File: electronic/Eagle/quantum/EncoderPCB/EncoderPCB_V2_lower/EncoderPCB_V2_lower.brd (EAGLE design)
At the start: 150 x 30 mm, 20 parts, among them IC1 STM32F031K6T6

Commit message: progress on parametricEQ
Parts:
- added C5, C6, C7: 100nF, C_Sager_Bibliothek:C0603
- added C8: 10 uF, passive components:C1206
- added IC2: STM32F031K6T6, C_Sager_Bibliothek:QFP80P900X900X160-32N
- added PRG-CONN1: 90814-0204, electro_mechanical:MOLEX_90814-0204
- added R5, R6: 10k, passive components:R0603
- moved PRG-CONN 139.2 mm to (8.50, 23.9), flipped to the top, turned to 180 degrees
- moved I2C-CONN 96.8 mm to (38.7, 42.9), flipped to the top, turned to 180 degrees
- moved C3 26.4 mm to (128.8, 19.8), flipped to the top
- moved R8 25.8 mm to (81.5, 21.9), flipped to the top
- moved R9 25.8 mm to (78.3, 21.7), flipped to the top
- moved R10 25.8 mm to (73.4, 22.0), flipped to the top
- moved C1 25.3 mm to (115.5, 14.0), flipped to the top
- moved C2 25.3 mm to (116.1, 18.6), flipped to the top
- moved IC1 25.3 mm to (122.3, 17.2), flipped to the top
- moved R1 25.3 mm to (115.5, 16.0), flipped to the top
- moved C4 25.2 mm to (114.0, 19.3), flipped to the top
- moved R2 20.2 mm to (68.4, 21.7), flipped to the top
- moved R4 20.2 mm to (62.2, 21.8), flipped to the top
- moved R3 20.2 mm to (65.4, 21.9), flipped to the top
- moved R11 20.0 mm to (124.5, 10.6), flipped to the top
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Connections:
- net +3V3: now also C5.1, C6.1, C7.1, C8.1, IC2.1, IC2.17, IC2.5
- net ADRR.: now also IC2.3, R5.2
- net BOOT_0: now also IC2.31, R6.2
- net BUTTON_ENC1: now also IC2.28
- net BUTTON_ENC2: now also IC2.30
- net BUTTON_ENC3: now also IC2.2
- net B_ENC1: now also IC2.11
- net B_ENC2: now also IC2.14
- net B_ENC3: now also IC2.27
- net ENCODER1_A: now also IC2.18
- net ENCODER1_B: now also IC2.19
- net ENCODER2_A: now also IC2.6
- net ENCODER2_B: now also IC2.7
- net ENCODER3_A: now also IC2.12
- net ENCODER3_B: now also IC2.13
- net GND: now also C5.2, C6.2, C7.2, C8.2, IC2.16, IC2.32, PRG-CONN1.4, R5.1, R6.1
- net G_ENC1: now also IC2.10
- net G_ENC2: now also IC2.22
- net G_ENC3: now also IC2.26
- net I2C1_SCL: now also IC2.29
- net I2C1_SDA: now also IC2.20
- net NRST: now also IC2.4, PRG-CONN1.2
- net R_ENC1: now also IC2.9
- net R_ENC2: now also IC2.21
- net R_ENC3: now also IC2.15
- net SWCLK: now also IC2.24, PRG-CONN1.1
- net SWDIO: now also IC2.23, PRG-CONN1.3
- net USART1_RX1: now also IC2.25
- net USART1_TX: now also IC2.8
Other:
- board size 150 x 30 mm -> 130 x 45 mm

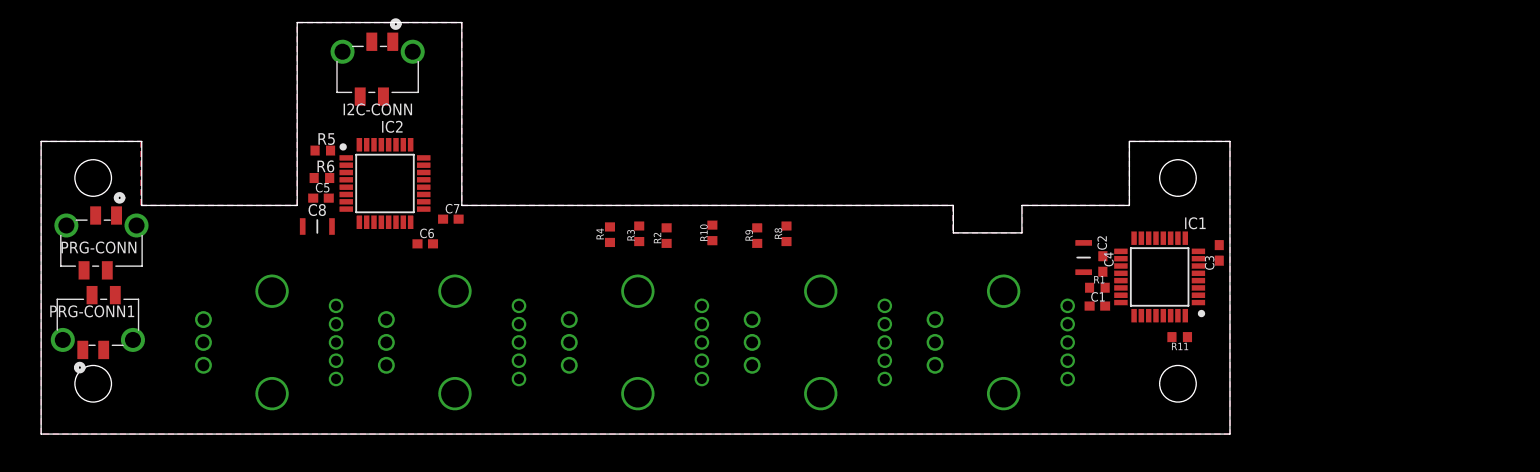
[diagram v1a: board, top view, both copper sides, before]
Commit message: finished EncoderPCB, Implemented Float OSC
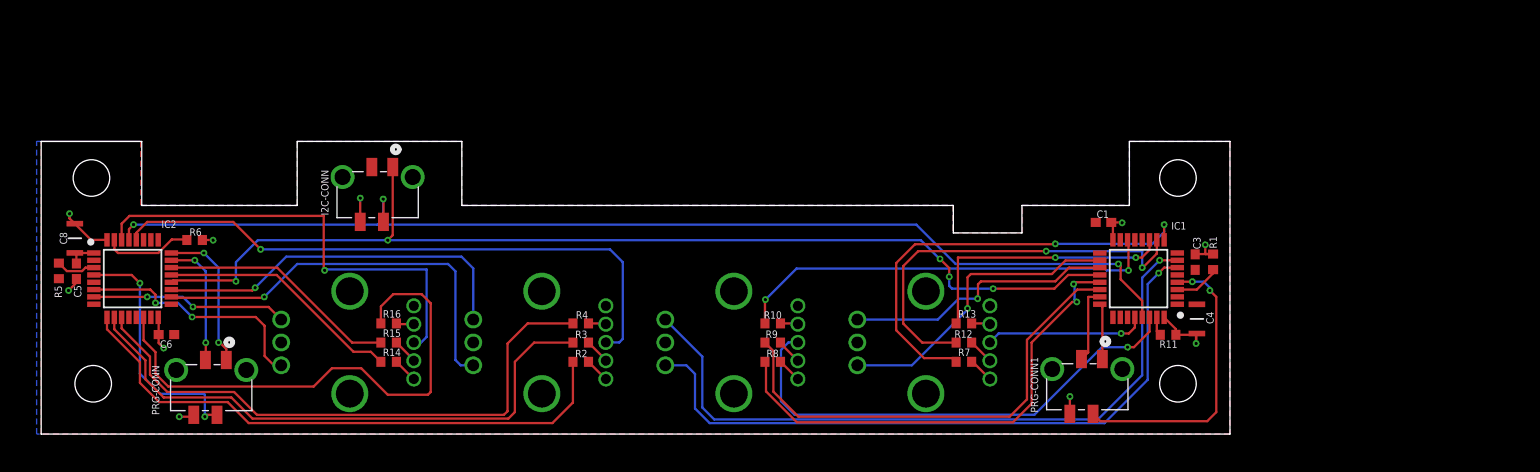
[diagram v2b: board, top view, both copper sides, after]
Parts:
- removed C2, C7: 100nF, C_Sager_Bibliothek:C0603
- removed S5: PEL12T-4225S-S1024, electro_mechanical:PEL12T4225SS1024
- added R12, R13, R14, R15, R16, R7: 51 R, passive components:R0603
- moved PRG-CONN1 112.0 mm to (116.3, 8.20), turned to 180 degrees
- moved S4 71.5 mm to (33.5, 10.0)
- moved R5 31.7 mm to (1.94, 17.8), turned to 90 degrees
- moved S1 31.5 mm to (96.5, 10.0)
- moved S2 30.5 mm to (75.5, 10.0)
- moved S3 30.5 mm to (54.5, 10.0)
- moved C6 30.0 mm to (13.7, 10.9), turned to 180 degrees
- moved IC2 29.5 mm to (10.0, 17.0)
- moved C5 27.9 mm to (3.85, 17.8), turned to 270 degrees
- moved C8 26.6 mm to (3.68, 21.4), turned to 90 degrees
- moved PRG-CONN 19.8 mm to (20.5, 8.10)
- moved R2 16.7 mm to (59.0, 7.90), turned to 0 degrees
- moved R6 15.5 mm to (16.8, 21.2), turned to 180 degrees
- moved C4 14.1 mm to (126.4, 12.6), turned to 270 degrees
- moved R8 14.1 mm to (80.0, 7.90), turned to 0 degrees
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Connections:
- removed net ADRR.: IC1.3, IC2.3, R1.2, R5.2
- removed net BOOT_0: IC1.31, IC2.31, R11.2, R6.2
- removed net BUTTON_ENC1: IC1.28, IC2.28, S1.3
- removed net BUTTON_ENC2: IC1.30, IC2.30
- removed net BUTTON_ENC3: IC1.2, IC2.2, S3.3
- removed net B_ENC1: IC1.11, IC2.11, R4.1
- removed net B_ENC2: IC1.14, IC2.14
- removed net B_ENC3: IC1.27, IC2.27, R10.1
- removed net ENCODER1_A: IC1.18, IC2.18, S1.A1
- removed net ENCODER1_B: IC1.19, IC2.19, S1.B1
- removed net ENCODER2_A: IC1.6, IC2.6
- removed net ENCODER2_B: IC1.7, IC2.7
- removed net ENCODER3_A: IC1.12, IC2.12, S3.A1
- removed net ENCODER3_B: IC1.13, IC2.13, S3.B1
- removed net G_ENC1: IC1.10, IC2.10, R3.1
- removed net G_ENC2: IC1.22, IC2.22
- removed net G_ENC3: IC1.26, IC2.26, R9.1
- removed net NRST: IC1.4, IC2.4, PRG-CONN.2, PRG-CONN1.2
- removed net R_ENC1: IC1.9, IC2.9, R2.1
- removed net R_ENC2: IC1.21, IC2.21
- removed net R_ENC3: IC1.15, IC2.15, R8.1
- removed net SWCLK: IC1.24, IC2.24, PRG-CONN.1, PRG-CONN1.1
- removed net SWDIO: IC1.23, IC2.23, PRG-CONN.3, PRG-CONN1.3
- removed net USART1_RX1: IC1.25, IC2.25
- removed net USART1_TX: IC1.8, IC2.8
- new net A_ADRR.: IC1.3, R1.2
- new net A_BOOT_0: IC1.31, R11.2
- new net A_BUTTON_ENC1: IC1.28, S1.3
- new net A_BUTTON_ENC2: IC1.30, S2.3
- new net A_BUTTON_ENC3: IC1.2
- new net A_B_ENC1: IC1.11, R13.1
- new net A_B_ENC2: IC1.14, R10.1
- new net A_B_ENC3: IC1.27
- new net A_ENCODER1_A: IC1.18, S1.A1
- new net A_ENCODER1_B: IC1.19, S1.B1
- new net A_ENCODER2_A: IC1.6, S2.A1
- new net A_ENCODER2_B: IC1.7, S2.B1
- new net A_ENCODER3_A: IC1.12
- new net A_ENCODER3_B: IC1.13
- new net A_G_ENC1: IC1.10, R12.1
- new net A_G_ENC2: IC1.22, R9.1
- new net A_G_ENC3: IC1.26
- new net A_NRST: IC1.4, PRG-CONN1.2
- new net A_R_ENC1: IC1.9, R7.1
- new net A_R_ENC2: IC1.21, R8.1
- new net A_R_ENC3: IC1.15
- new net A_SWCLK: IC1.24, PRG-CONN1.1
- new net A_SWDIO: IC1.23, PRG-CONN1.3
- new net A_USART1_RX: IC1.25
- new net A_USART1_TX: IC1.8
- new net B_ADRR.: IC2.3, R5.2
- new net B_BOOT_0: IC2.31, R6.2
- new net B_BUTTON_ENC1: IC2.28, S3.3
- new net B_BUTTON_ENC2: IC2.30, S4.3
- new net B_BUTTON_ENC3: IC2.2
- new net B_B_ENC1: IC2.11, R4.1
- new net B_B_ENC2: IC2.14, R16.1
- new net B_B_ENC3: IC2.27
- new net B_ENCODER1_A: IC2.18, S3.A1
- new net B_ENCODER1_B: IC2.19, S3.B1
- new net B_ENCODER2_A: IC2.6, S4.A1
- new net B_ENCODER2_B: IC2.7, S4.B1
- new net B_ENCODER3_A: IC2.12
- new net B_ENCODER3_B: IC2.13
- new net B_G_ENC1: IC2.10, R3.1
- new net B_G_ENC2: IC2.22, R15.1
- new net B_G_ENC3: IC2.26
- new net B_NRST: IC2.4, PRG-CONN.2
- new net B_R_ENC1: IC2.9, R2.1
- new net B_R_ENC2: IC2.21, R14.1
- new net B_R_ENC3: IC2.15
- new net B_SWCLK: IC2.24, PRG-CONN.1
- new net B_SWDIO: IC2.23, PRG-CONN.3
- new net B_USART1_RX: IC2.25
- new net B_USART1_TX: IC2.8
- new net N$1: R7.2, S1.1
- new net N$2: R12.2, S1.2
- new net N$3: R13.2, S1.4
- new net N$4: R14.2, S4.1
- new net N$5: R15.2, S4.2
- new net N$6: R16.2, S4.4
- net +3V3: now also R5.1, S2.5, S4.5; no longer C2.1, C7.1
- net GND: now also S2.C1, S4.C1; no longer C2.2, C7.2, R5.1
- net N$10: now also S3.2; no longer S1.2
- net N$12: now also S3.4; no longer S1.4
- net N$15: now also S2.1; no longer S3.1
- net N$16: now also S2.2; no longer S3.2
- net N$17: now also S2.4; no longer S3.4
- net N$9: now also S3.1; no longer S1.1
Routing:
- net I2C1_SCL: track 0.00 -> 123.8 mm, vias 0 -> 3
- net I2C1_SDA: track 0.00 -> 117.0 mm, vias 0 -> 5
- net A_ENCODER2_B: track 0.00 -> 77.2 mm, vias 0 -> 1
- net A_ENCODER2_A: track 0.00 -> 74.0 mm, vias 0 -> 1
- net B_BUTTON_ENC1: track 0.00 -> 66.7 mm, vias 0 -> 1
- net B_B_ENC1: track 0.00 -> 64.1 mm
- net B_G_ENC1: track 0.00 -> 63.4 mm
- net B_R_ENC1: track 0.00 -> 63.2 mm
- net B_B_ENC2: track 0.00 -> 57.5 mm
- net A_BUTTON_ENC2: track 0.00 -> 54.0 mm, vias 0 -> 1
- net A_R_ENC2: track 0.00 -> 53.1 mm, vias 0 -> 2
- net A_G_ENC2: track 0.00 -> 52.1 mm
- net B_BUTTON_ENC2: track 0.00 -> 50.4 mm, vias 0 -> 1
- net A_R_ENC1: track 0.00 -> 48.5 mm, vias 0 -> 2
- net A_B_ENC2: track 0.00 -> 47.2 mm, vias 0 -> 2
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- added copper zone on layer 1, net +3V3
- added copper zone on layer 16, net GND
- removed copper zone on layer 16, net +3V3
- removed copper zone on layer 1, net GND
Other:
- board size 130 x 45 mm -> 130 x 32 mm
